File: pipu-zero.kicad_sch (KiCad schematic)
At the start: 4 parts, among them J1 USB_C_Receptacle_USB2.0_14P

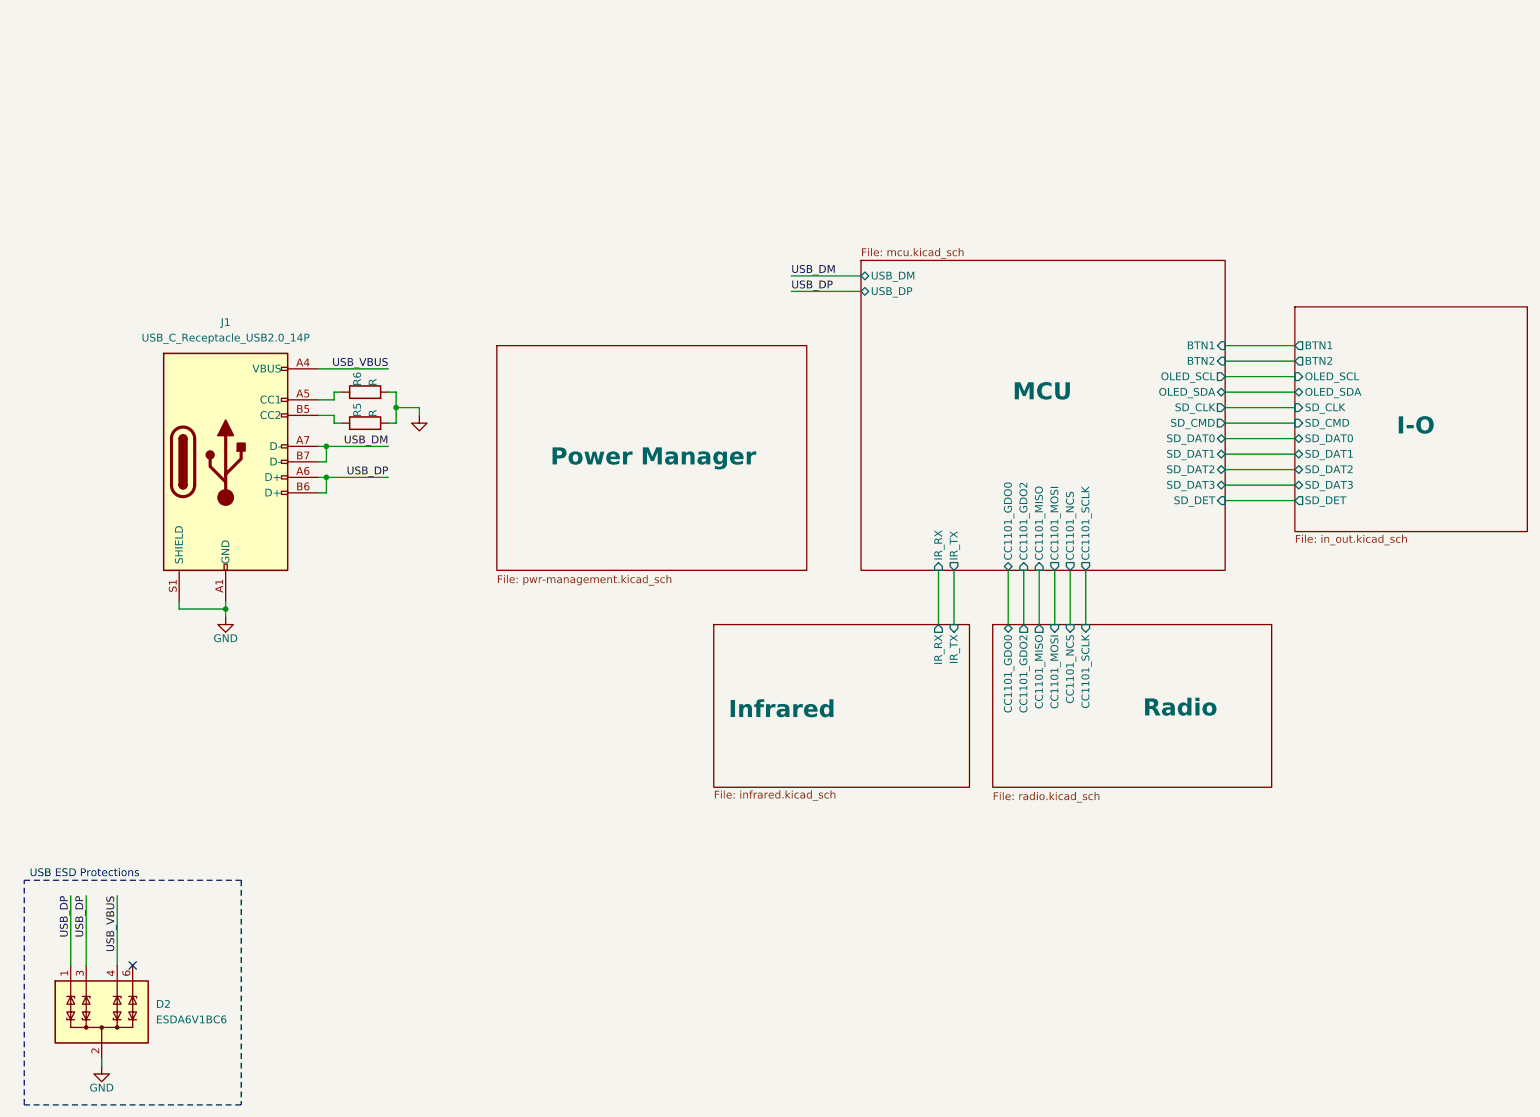
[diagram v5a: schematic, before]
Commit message: fix rgb led labels
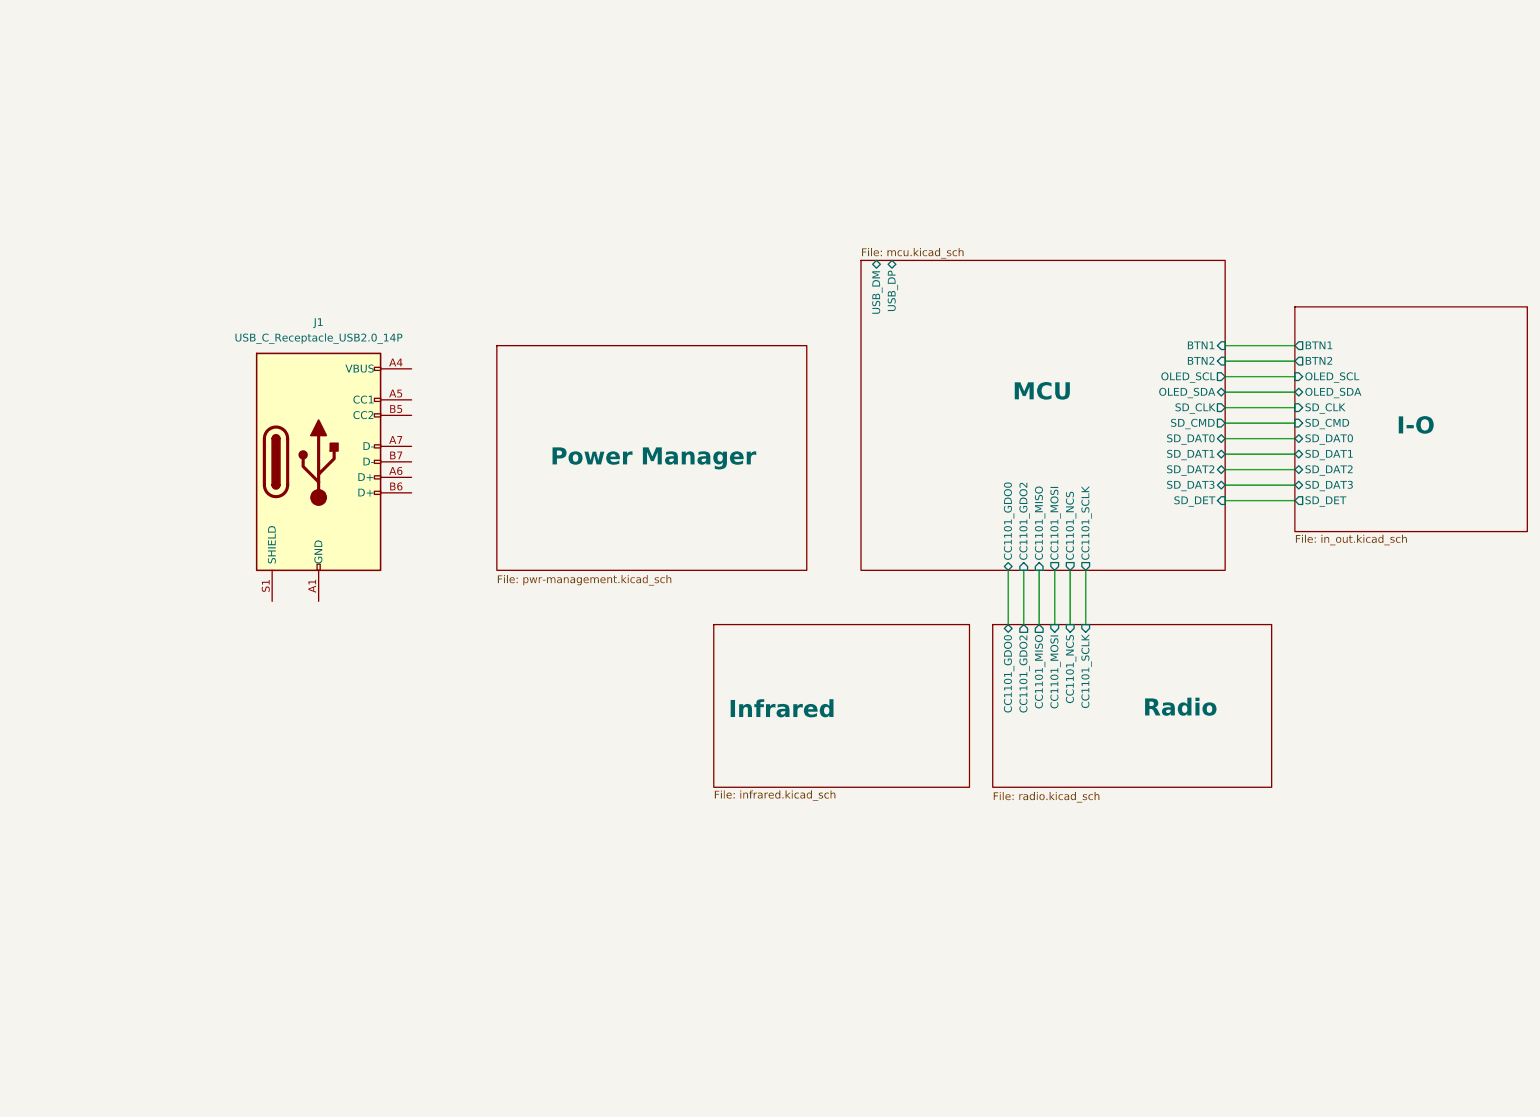
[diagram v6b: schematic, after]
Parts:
- removed D2: ESDA6V1BC6, Package_TO_SOT_SMD:SOT-23-6, symbol Power_Protection:ESDA6V1BC6
- removed R5, R6: R, symbol Device:R
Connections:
- net GND: no longer names the net of J1.A1 (GND), J1.A12 (GND), J1.B1 (GND), J1.B12 (GND)
- net GND: no longer J1.S1 (SHIELD)
- net USB_DM: no longer names the net of J1.A7 (D-)
- net USB_DM: no longer J1.B7 (D-)
- net USB_DP: no longer names the net of J1.A6 (D+)
- net USB_DP: no longer J1.B6 (D+)
- net USB_VBUS: no longer names the net of J1.A4 (VBUS), J1.A9 (VBUS), J1.B4 (VBUS), J1.B9 (VBUS)
- no-connect marks 1 -> 0
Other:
- sheet Infrared ports: added none; removed IR_RX, IR_TX
- sheet MCU ports: added none; removed IR_RX, IR_TX
- note removed: "USB ESD Protections"
- moved on the sheet: J1

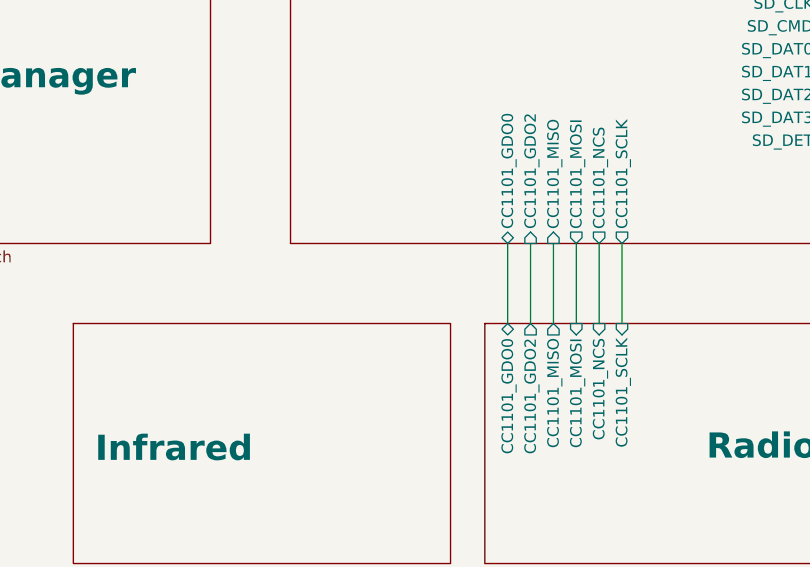
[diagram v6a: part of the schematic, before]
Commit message: add external gpio connector
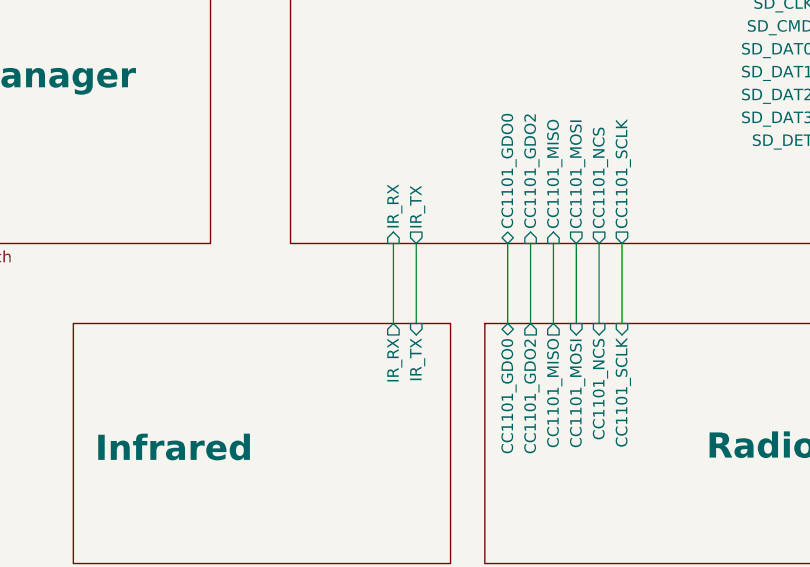
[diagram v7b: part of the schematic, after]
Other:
- sheet Infrared ports: added IR_RX, IR_TX; removed none
- sheet MCU ports: added IR_RX, IR_TX; removed none
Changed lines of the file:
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@@
+	(wire
+		(pts
+			(xy 165.1 106.68) (xy 165.1 115.57)
+		)
+		(stroke
+			(width 0)
+			(type default)
+		)
+	)
 	(wire
 		(pts
@@
 		(pts
 			(xy 182.88 106.68) (xy 182.88 115.57)
+		)
+		(stroke
+			(width 0)
+			(type default)
+		)
+	)
+	(wire
+		(pts
+			(xy 167.64 106.68) (xy 167.64 115.57)
 		)
 		(stroke
@@
 			)
 		)
+		(pin "IR_RX" input
+			(at 165.1 106.68 270)
+			(effects
+				(font
+					(size 1.27 1.27)
+				)
+				(justify left)
+			)
+		)
+		(pin "IR_TX" output
+			(at 167.64 106.68 270)
+			(effects
+				(font
+					(size 1.27 1.27)
+				)
+				(justify left)
+			)
+		)
 		(instances
 			(project "pipu-zero"
@@
 			)
 		)
+		(pin "IR_RX" output
+			(at 165.1 115.57 90)
+			(effects
+				(font
+					(size 1.27 1.27)
+				)
+				(justify right)
+			)
+		)
+		(pin "IR_TX" input
+			(at 167.64 115.57 90)
+			(effects
+				(font
+					(size 1.27 1.27)
+				)
+				(justify right)
+			)
+		)

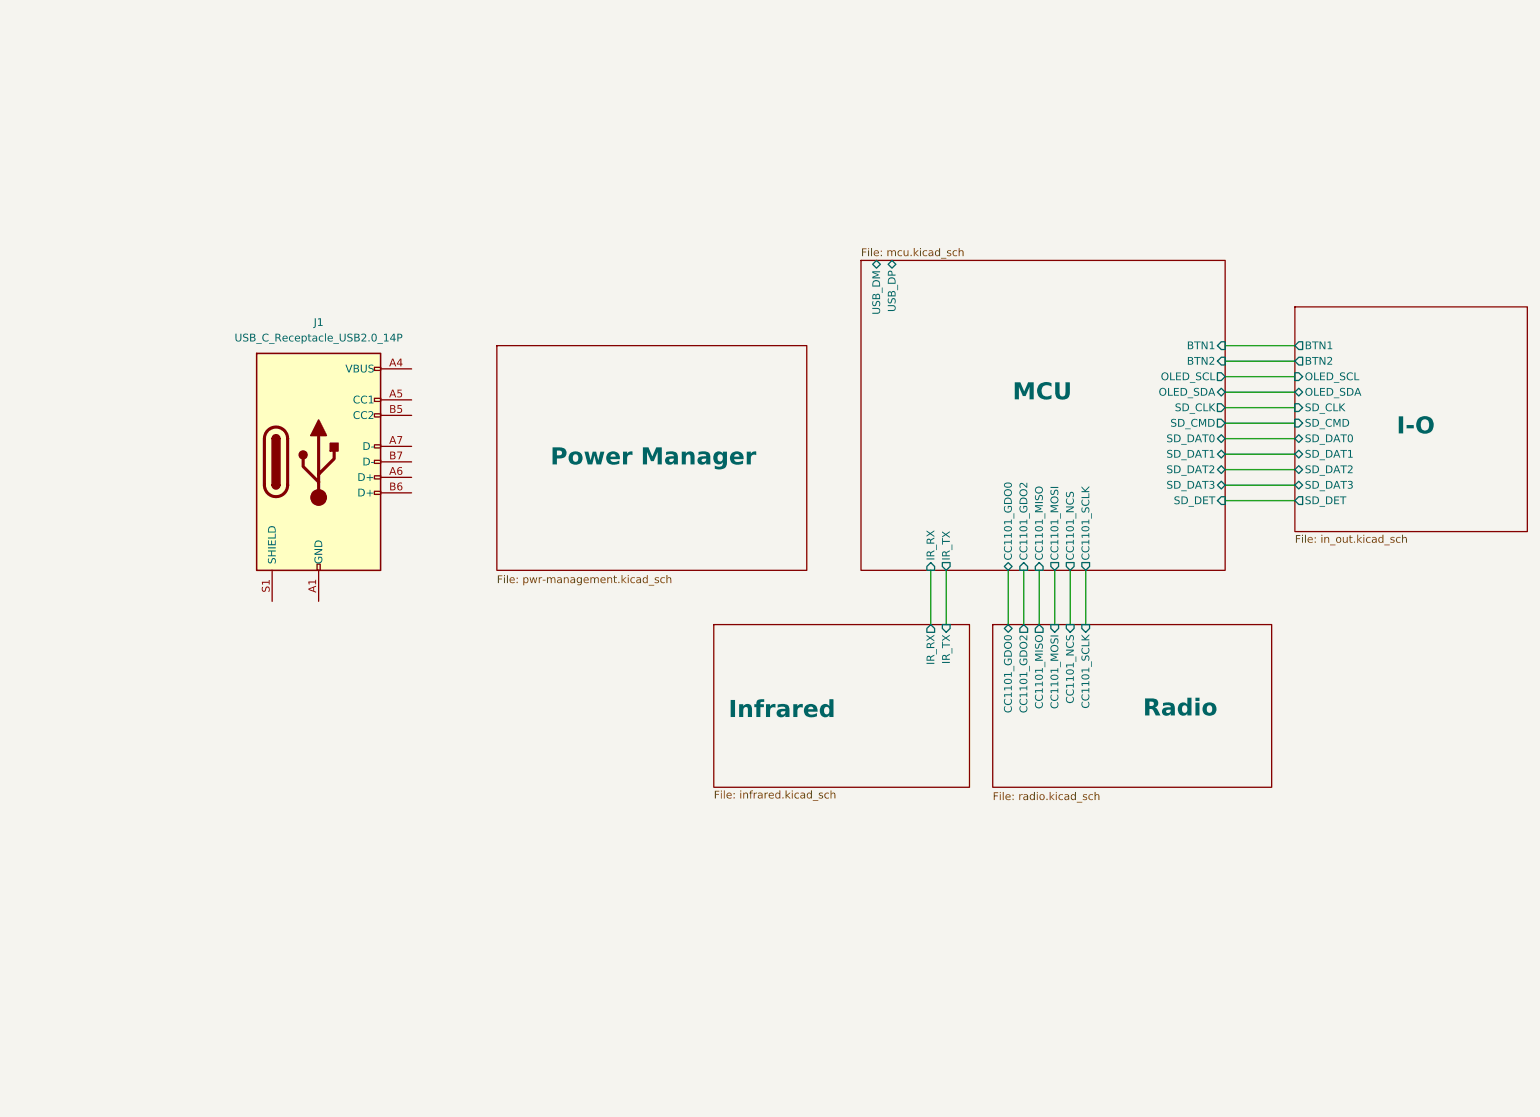
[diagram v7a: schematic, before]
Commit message: add usbc esd protections
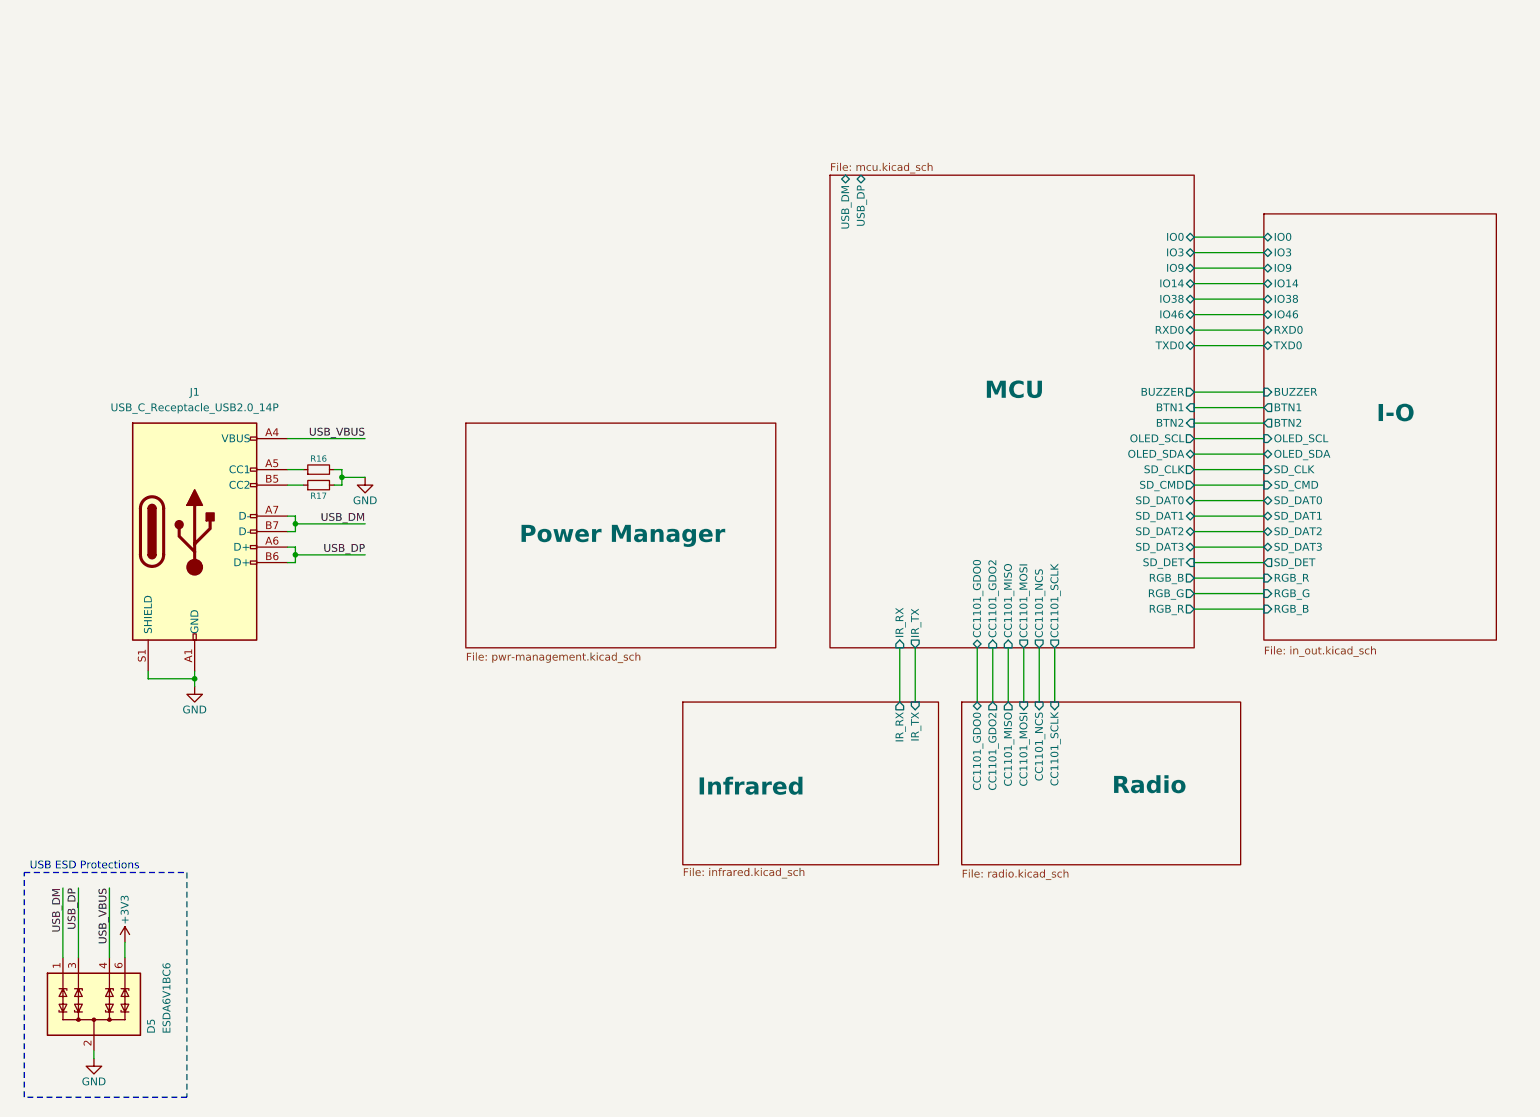
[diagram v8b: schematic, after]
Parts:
- added D5: ESDA6V1BC6, Package_TO_SOT_SMD:SOT-23-6, symbol Power_Protection:ESDA6V1BC6
- added R16, R17: R_Small, symbol Device:R_Small
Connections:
- net GND: now reaches J1.A1 (GND), J1.A12 (GND), J1.B1 (GND), J1.B12 (GND)
- net GND: now also J1.S1 (SHIELD), D5.2 (COM), D5.5 (COM), R16.2, R17.2
- net USB_VBUS: now reaches J1.A4 (VBUS), J1.A9 (VBUS), J1.B4 (VBUS), J1.B9 (VBUS)
- net USB_VBUS: now also D5.4 (TVS3)
- net at J1.A5 (CC1): now also R16.1
- net USB_DP: now reaches J1.A6 (D+)
- net USB_DP: now also J1.B6 (D+), D5.3 (TVS2)
- net USB_DM: now reaches J1.A7 (D-)
- net USB_DM: now also J1.B7 (D-), D5.1 (TVS1)
- net at J1.B5 (CC2): now also R17.1
- new net +3V3: D5.6 (TVS4)
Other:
- sheet I-O ports: added BUZZER, IO0, IO14, IO3, IO38, IO46, IO9, RGB_B, RGB_G, RGB_R, RXD0, TXD0; removed none
- sheet MCU ports: added BUZZER, IO0, IO14, IO3, IO38, IO46, IO9, RGB_B, RGB_G, RGB_R, RXD0, TXD0; removed none
- note added: "USB ESD Protections"
- moved on the sheet: J1
